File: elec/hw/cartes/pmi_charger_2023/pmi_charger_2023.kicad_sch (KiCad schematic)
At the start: 35 parts, among them J1 BTC-TC6S-23, SW1 MSS12C02LS-BB2.0, SW2 MSS12C02LS-BB2.0, U1 BQ25308RTER

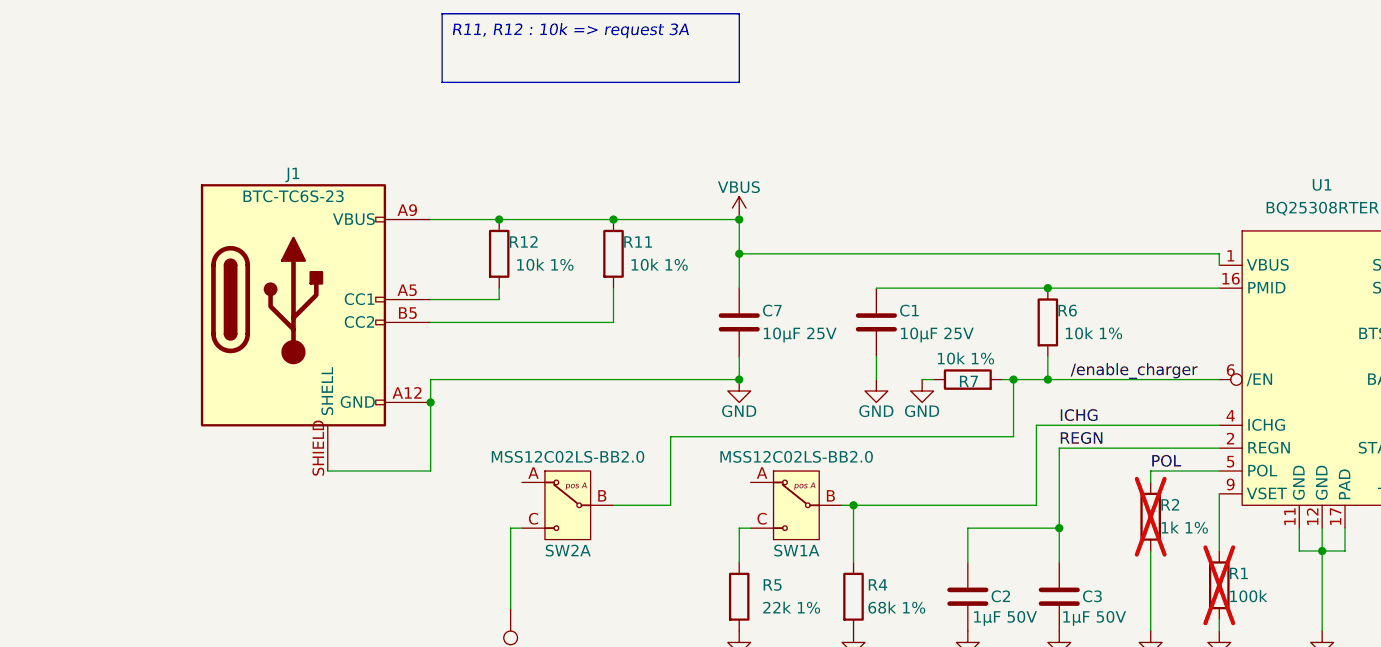
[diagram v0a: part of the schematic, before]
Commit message: fix:CC1/CC2 corrected, R6 connected to VBUS, R7 : set to unmounted
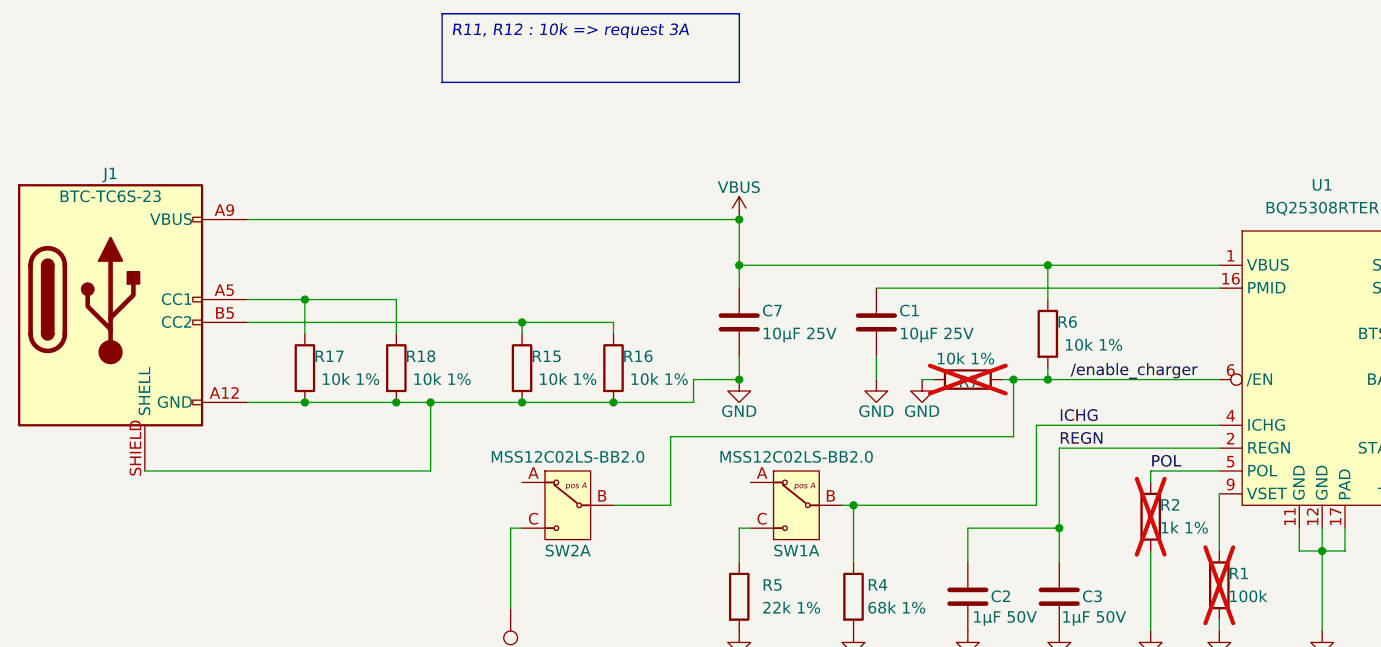
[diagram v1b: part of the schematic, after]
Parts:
- removed R11, R12: 10k 1%, cocotter_resistor:r0603_reflow, symbol cocotter_resistors:R_10k_0603_1%
- added R15, R16, R17, R18: 10k 1%, cocotter_resistor:r0603_reflow, symbol cocotter_resistors:R_10k_0603_1%
- R7: now not fitted
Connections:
- net GND: now also R15.2, R16.2, R17.2, R18.2
- net VBUS: now also R6.1
- net at C1.1, U1.16 (PMID): no longer R6.1
- net at J1.A5 (CC1): now also R17.1, R18.1
- net at J1.B5 (CC2): now also R15.1, R16.1
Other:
- moved on the sheet: J1, R6
